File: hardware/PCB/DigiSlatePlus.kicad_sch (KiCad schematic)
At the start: 43 parts, among them J1 Serial, J10 IO7, J2 USB_B, J6 Mains, J7 Timecode IN, J8 Timecode OUT, J9 MISO, Q4 2N2222, SW1 RotaryEncoder-SW, SW2 1, SW3 1, SW4 1, SW5 1, SW6 BOOT, U1 ESP32-S3-WROOM-1, U2 DS3231M

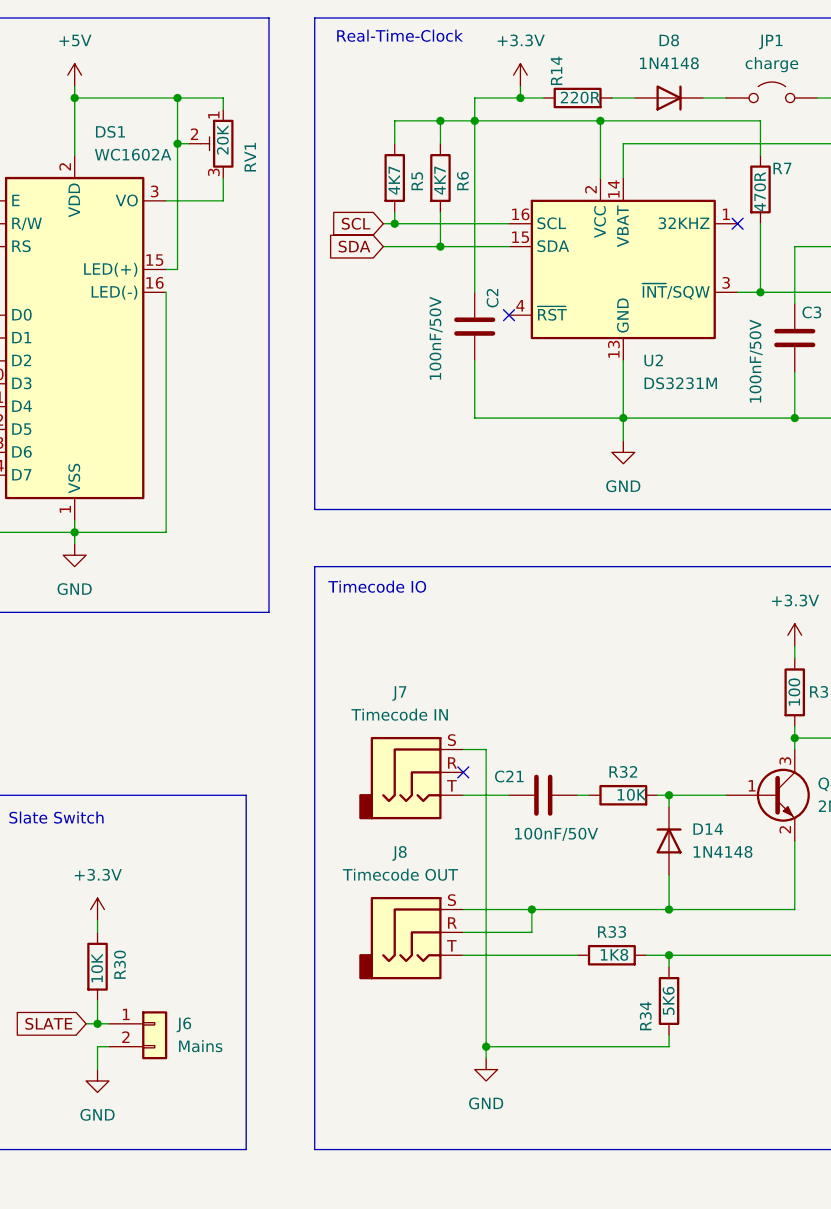
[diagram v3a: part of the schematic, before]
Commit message: minor bugfixes in schematics and board
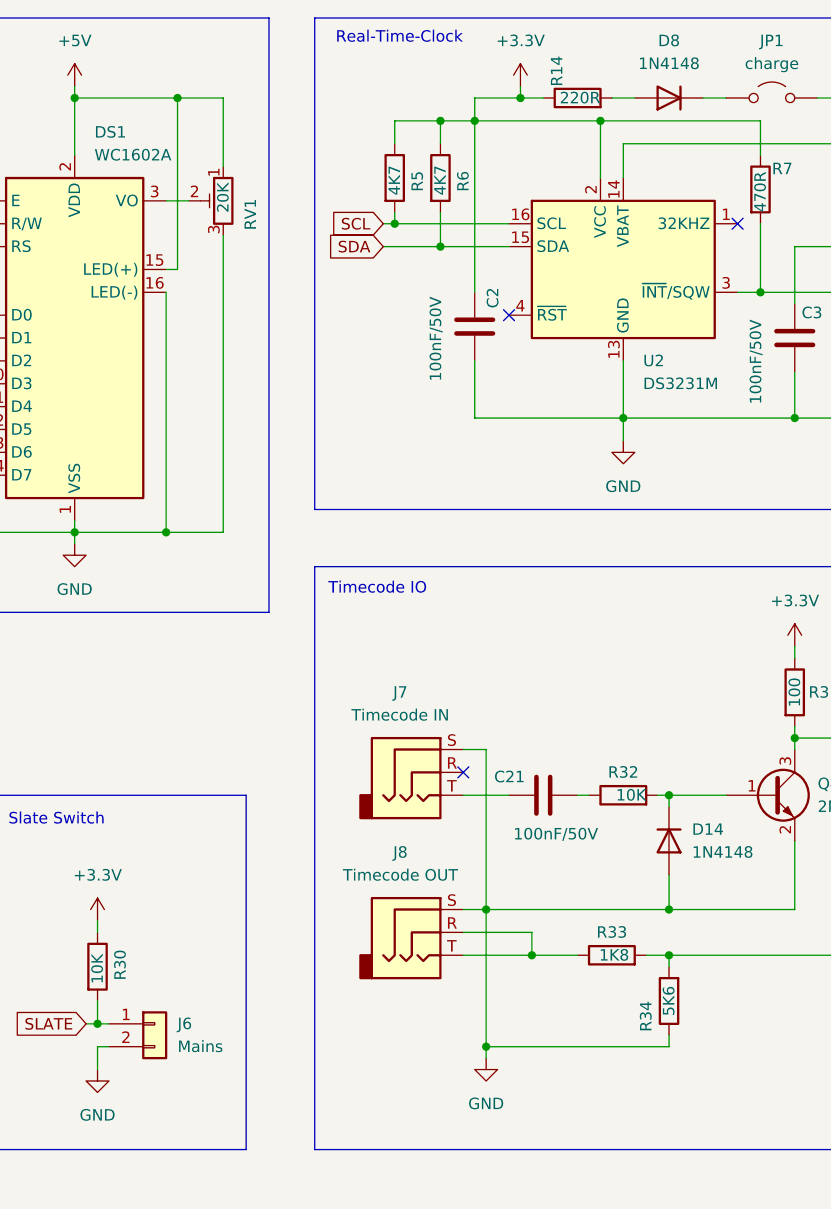
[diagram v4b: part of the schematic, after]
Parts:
- J2: footprint Connector_USB:USB_B_Lumberg_2411_02_Horizontal -> USB-B:USB_B_Lumberg_2411_02_Horizontal
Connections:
- net +5V: no longer RV1.2
- net GND: now also D14.2 (A), J8.S, Q4.2 (E), RV1.3
- net at DS1.3 (VO): now also RV1.2; no longer RV1.3
- net at J8.T, R33.1: now also J8.R
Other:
- moved on the sheet: RV1
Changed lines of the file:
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@@
 	)
 	(junction
+		(at 207.01 127)
+		(diameter 0)
+		(color 0 0 0 0)
+	)
+	(junction
 		(at 139.7 125.73)
 		(diameter 0)
@@
 	)
 	(junction
+		(at 212.09 132.08)
+		(diameter 0)
+		(color 0 0 0 0)
+	)
+	(junction
 		(at 77.47 134.62)
 		(diameter 0)
@@
 	)
 	(junction
-		(at 172.72 41.91)
+		(at 171.45 85.09)
 		(diameter 0)
 		(color 0 0 0 0)
@@
 	)
 	(junction
-		(at 212.09 127)
-		(diameter 0)
-		(color 0 0 0 0)
-	)
-	(junction
 		(at 67.31 36.83)
 		(diameter 0)
@@
 	(wire
 		(pts
-			(xy 177.8 38.1) (xy 177.8 36.83)
+			(xy 177.8 52.07) (xy 177.8 85.09)
+		)
+		(stroke
+			(width 0)
+			(type default)
+		)
+	)
+	(wire
+		(pts
+			(xy 177.8 44.45) (xy 177.8 36.83)
 		)
 		(stroke
@@
 	(wire
 		(pts
-			(xy 212.09 129.54) (xy 212.09 127)
-		)
-		(stroke
-			(width 0)
-			(type default)
-		)
-	)
-	(wire
-		(pts
 			(xy 73.66 139.7) (xy 76.2 139.7)
 		)
@@
 	(wire
 		(pts
-			(xy 177.8 45.72) (xy 177.8 48.26)
-		)
-		(stroke
-			(width 0)
-			(type default)
-		)
-	)
-	(wire
-		(pts
 			(xy 227.33 132.08) (xy 227.33 133.35)
 		)
@@
 	(wire
 		(pts
+			(xy 207.01 127) (xy 207.01 142.24)
+		)
+		(stroke
+			(width 0)
+			(type default)
+		)
+	)
+	(wire
+		(pts
 			(xy 67.31 99.06) (xy 67.31 97.79)
 		)
@@
 	(wire
 		(pts
-			(xy 172.72 41.91) (xy 172.72 36.83)
+			(xy 172.72 36.83) (xy 172.72 55.88)
 		)
 		(stroke
@@
 	(wire
 		(pts
-			(xy 227.33 127) (xy 212.09 127)
+			(xy 201.93 39.37) (xy 205.74 39.37)
 		)
 		(stroke
@@
 	(wire
 		(pts
-			(xy 201.93 39.37) (xy 205.74 39.37)
+			(xy 205.74 66.04) (xy 205.74 72.39)
 		)
 		(stroke
@@
 	(wire
 		(pts
-			(xy 205.74 66.04) (xy 205.74 72.39)
+			(xy 45.72 134.62) (xy 52.07 134.62)
 		)
 		(stroke
@@
 	(wire
 		(pts
-			(xy 45.72 134.62) (xy 52.07 134.62)
+			(xy 212.09 132.08) (xy 217.17 132.08)
 		)
 		(stroke
@@
 	(wire
 		(pts
-			(xy 204.47 127) (xy 212.09 127)
+			(xy 204.47 127) (xy 207.01 127)
 		)
 		(stroke
@@
 	(wire
 		(pts
+			(xy 177.8 85.09) (xy 171.45 85.09)
+		)
+		(stroke
+			(width 0)
+			(type default)
+		)
+	)
+	(wire
+		(pts
 			(xy 45.72 46.99) (xy 49.53 46.99)
 		)
@@
 	(wire
 		(pts
-			(xy 207.01 109.22) (xy 207.01 142.24)
+			(xy 207.01 109.22) (xy 207.01 127)
+		)
+		(stroke
+			(width 0)
+			(type default)
+		)
+	)
+	(wire
+		(pts
+			(xy 171.45 48.26) (xy 173.99 48.26)
 		)
 		(stroke
@@
 	(wire
 		(pts
-			(xy 177.8 48.26) (xy 171.45 48.26)
+			(xy 120.65 49.53) (xy 121.92 49.53)
 		)
 		(stroke
@@
 	(wire
 		(pts
-			(xy 120.65 49.53) (xy 121.92 49.53)
+			(xy 207.01 127) (xy 227.33 127)
+		)
+		(stroke
+			(width 0)
+			(type default)
+		)
+	)
+	(wire
+		(pts
+			(xy 212.09 129.54) (xy 212.09 132.08)
 		)
 		(stroke
@@
 	(wire
 		(pts
-			(xy 204.47 132.08) (xy 217.17 132.08)
+			(xy 204.47 132.08) (xy 212.09 132.08)
 		)
 		(stroke
@@
 	(wire
 		(pts
-			(xy 173.99 41.91) (xy 172.72 41.91)
-		)
-		(stroke
-			(width 0)
-			(type default)
-		)
-	)
-	(wire
-		(pts
 			(xy 115.57 86.36) (xy 118.11 86.36)
 		)
@@
 	(wire
 		(pts
-			(xy 172.72 55.88) (xy 172.72 41.91)
-		)
-		(stroke
-			(width 0)
-			(type default)
-		)
-	)
-	(wire
-		(pts
 			(xy 38.1 99.06) (xy 67.31 99.06)
 		)
@@
 	(symbol
 		(lib_id "Device:R_Potentiometer_Trim")
-		(at 177.8 41.91 0)
+		(at 177.8 48.26 0)
 		(mirror y)
 		(unit 1)
@@
 		(dnp no)
 		(property "Reference" "RV1"
-			(at 180.848 41.656 90)
+			(at 180.848 48.006 90)
 			(effects
 				(font
@@
 		)
 		(property "Value" "20K"
-			(at 177.8 39.878 90)
+			(at 177.8 46.228 90)
 			(effects
 				(font
@@
 		)
 		(property "Footprint" "Potentiometer_SMD:Potentiometer_Vishay_TS53YL_Vertical"
-			(at 177.8 41.91 0)
+			(at 177.8 48.26 0)
 			(effects
 				(font
@@
 		)
 		(property "Datasheet" "~"
-			(at 177.8 41.91 0)
+			(at 177.8 48.26 0)
 			(effects
 				(font
@@
 		)
 		(property "Description" "Trim-potentiometer"
-			(at 177.8 41.91 0)
+			(at 177.8 48.26 0)
 			(effects
 				(font
@@
 			)
 		)
-		(property "Footprint" "Connector_USB:USB_B_Lumberg_2411_02_Horizontal"
+		(property "Footprint" "USB-B:USB_B_Lumberg_2411_02_Horizontal"
 			(at 121.92 76.2 0)
 			(effects

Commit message: new harware bugfixes while building the prototype
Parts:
- added C40: 100nF/50V, Capacitor_SMD:C_1206_3216Metric_Pad1.33x1.80mm_HandSolder, symbol Device:C
- R31: value 100 -> 10k
- RV1: value 20K -> 10K
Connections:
- net RST: now also C40.1; no longer R1.2, U1.3 (EN)
- net SCL: no longer U2.16 (SCL)
- new net: C40.2, R1.2, U1.3 (EN)
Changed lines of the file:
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@@
 		(title "DigiSlate+")
 		(date "2024-09-05")
-		(rev "1.0")
+		(rev "1.1")
 	)
 	(junction
@@
 	)
 	(junction
-		(at 196.85 50.8)
-		(diameter 0)
-		(color 0 0 0 0)
-	)
-	(junction
 		(at 161.29 85.09)
 		(diameter 0)
@@
 	(wire
 		(pts
+			(xy 44.45 46.99) (xy 49.53 46.99)
+		)
+		(stroke
+			(width 0)
+			(type default)
+		)
+	)
+	(wire
+		(pts
 			(xy 139.7 143.51) (xy 139.7 142.24)
 		)
@@
 	(wire
 		(pts
-			(xy 45.72 46.99) (xy 49.53 46.99)
+			(xy 34.29 46.99) (xy 36.83 46.99)
 		)
 		(stroke
@@
 	(wire
 		(pts
-			(xy 196.85 50.8) (xy 209.55 50.8)
+			(xy 209.55 38.1) (xy 209.55 50.8)
 		)
 		(stroke
@@
 	)
 	(rectangle
-		(start 33.02 27.94)
+		(start 18.415 27.94)
 		(end 105.41 107.95)
 		(stroke
@@
 	(global_label "RST"
 		(shape input)
-		(at 45.72 46.99 180)
+		(at 34.29 46.99 180)
 		(fields_autoplaced yes)
 		(effects
@@
 		)
 		(property "Intersheetrefs" "${INTERSHEET_REFS}"
-			(at 39.2877 46.99 0)
+			(at 27.8577 46.99 0)
 			(effects
 				(font
@@
 	)
 	(symbol
+		(lib_id "Device:C")
+		(at 40.64 46.99 90)
+		(unit 1)
+		(exclude_from_sim no)
+		(in_bom yes)
+		(on_board yes)
+		(dnp no)
+		(property "Reference" "C40"
+			(at 38.1 45.974 0)
+			(effects
+				(font
+					(size 1.27 1.27)
+				)
+				(justify left)
+			)
+		)
+		(property "Value" "100nF/50V"
+			(at 45.974 41.91 90)
+			(effects
+				(font
+					(size 1.27 1.27)
+				)
+				(justify left)
+			)
+		)
+		(property "Footprint" "Capacitor_SMD:C_1206_3216Metric_Pad1.33x1.80mm_HandSolder"
+			(at 44.45 46.0248 0)
+			(effects
+				(font
+					(size 1.27 1.27)
+				)
+				(hide yes)
+			)
+		)
+		(property "Datasheet" "~"
+			(at 40.64 46.99 0)
+			(effects
+				(font
+					(size 1.27 1.27)
+				)
+				(hide yes)
+			)
+		)
+		(property "Description" "Unpolarized capacitor"
+			(at 40.64 46.99 0)
+			(effects
+				(font
+					(size 1.27 1.27)
+				)
+				(hide yes)
+			)
+		)
+		(pin "1"
+		)
+		(pin "2"
+		)
+		(instances
+			(project "DigiSlatePlus"
+				(path "/dcb9cf24-5afa-4bbe-8afa-a00529143e4d"
+					(reference "C40")
+					(unit 1)
+				)
+			)
+		)
+	)
+	(symbol
 		(lib_id "power:GND")
 		(at 118.11 87.63 0)
@@
 			)
 		)
-		(property "Value" "20K"
+		(property "Value" "10K"
 			(at 177.8 46.228 90)
 			(effects
@@
 			)
 		)
-		(property "Value" "100"
+		(property "Value" "10k"
 			(at 241.3 102.87 90)
 			(effects

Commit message: KiCAD bagfix update
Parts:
- J6: value Mains -> Slate
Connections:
- net SCL: now also U2.16 (SCL)
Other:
- note added: "remove R3 for correct boot mode"
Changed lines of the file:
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@@
 	)
 	(junction
+		(at 196.85 50.8)
+		(diameter 0)
+		(color 0 0 0 0)
+	)
+	(junction
 		(at 161.29 85.09)
 		(diameter 0)
@@
 	(wire
 		(pts
+			(xy 196.85 50.8) (xy 209.55 50.8)
+		)
+		(stroke
+			(width 0)
+			(type default)
+		)
+	)
+	(wire
+		(pts
 			(xy 204.47 114.3) (xy 209.55 114.3)
 		)
@@
 	(wire
 		(pts
-			(xy 209.55 38.1) (xy 209.55 50.8)
-		)
-		(stroke
-			(width 0)
-			(type default)
-		)
-	)
-	(wire
-		(pts
 			(xy 49.53 46.99) (xy 52.07 46.99)
 		)
@@
 		)
 	)
+	(text "remove R3 for\ncorrect boot mode"
+		(exclude_from_sim no)
+		(at 43.688 147.574 0)
+		(effects
+			(font
+				(size 1.27 1.27)
+			)
+		)
+	)
 	(text "I/O"
 		(exclude_from_sim no)
@@
 			)
 		)
-		(property "Value" "Mains"
+		(property "Value" "Slate"
 			(at 172.72 142.2399 0)
 			(effects

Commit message: minor fixes on pcb
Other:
- note added: "remove R3 for serial boot mode"
- note removed: "remove R3 for correct boot mode"
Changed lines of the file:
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@@
 		)
 	)
-	(text "remove R3 for\ncorrect boot mode"
+	(text "remove R3 for\nserial boot mode"
 		(exclude_from_sim no)
 		(at 43.688 147.574 0)

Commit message: Last bug fixes
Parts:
- added D16: RX, LED_SMD:LED_0603_1608Metric, symbol Device:LED
- added D17: TX+, LED_SMD:LED_0603_1608Metric, symbol Device:LED
- added R37, R38: 180, Resistor_SMD:R_0805_2012Metric_Pad1.20x1.40mm_HandSolder, symbol Device:R
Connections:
- net GND: now also D16.1 (K), D17.1 (K)
- net RX0: now also R37.2
- net TX0: now also R38.2
- new net: D17.2 (A), R38.1
- new net: D16.2 (A), R37.1
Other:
- moved on the sheet: BT1, C2, C21, C3, D14, D8, DS1, J1, J10, J2, J7, J8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
